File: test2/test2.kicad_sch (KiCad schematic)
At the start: 2 parts

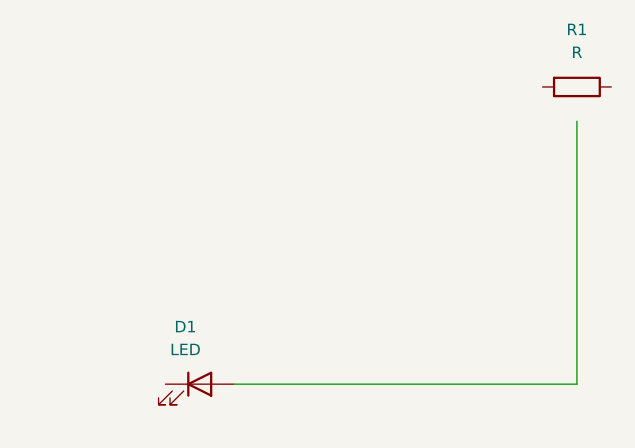
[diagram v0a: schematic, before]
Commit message: 2 Reference Changed and  1 value changed
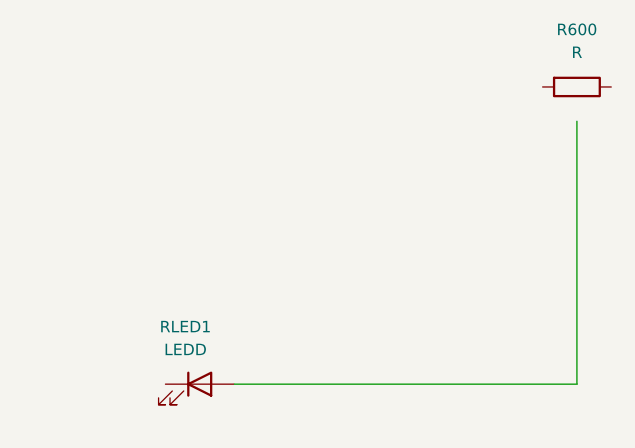
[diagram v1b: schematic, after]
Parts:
- RLED1: renamed from D1; value LED -> LEDD
- renumbered R1 to R600
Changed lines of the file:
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@@
 		(dnp no)
 		(fields_autoplaced yes)
-		(property "Reference" "R1"
+		(property "Reference" "R600"
 			(at 144.78 78.74 90)
 			(show_name no)
@@
 			(project "test2"
 				(path "/a16b2917-54e0-4f71-a869-9bcc0622af1e"
-					(reference "R1")
+					(reference "R600")
 					(unit 1)
 				)
@@
 		(dnp no)
 		(fields_autoplaced yes)
-		(property "Reference" "D1"
+		(property "Reference" "RLED1"
 			(at 101.2825 111.76 0)
 			(show_name no)
@@
 			)
 		)
-		(property "Value" "LED"
+		(property "Value" "LEDD"
 			(at 101.2825 114.3 0)
 			(show_name no)
@@
 			(project "test2"
 				(path "/a16b2917-54e0-4f71-a869-9bcc0622af1e"
-					(reference "D1")
+					(reference "RLED1")
 					(unit 1)
 				)

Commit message: Changed DNP in one changed footprint in other
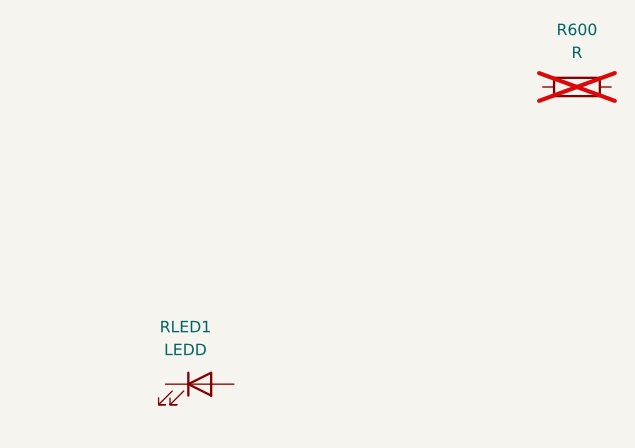
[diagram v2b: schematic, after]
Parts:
- R600: now not fitted; now left out of the parts list
- RLED1: footprint (none) -> Battery:BatteryClip_Keystone_54_D16-19mm
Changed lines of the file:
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@@
 		(comment 5 "c1000")
-	)
-	(wire
-		(pts
-			(xy 106.68 118.11) (xy 144.78 118.11)
-		)
-		(stroke
-			(width 0)
-			(type default)
-		)
-	)
-	(wire
-		(pts
-			(xy 144.78 118.11) (xy 144.78 88.9)
-		)
-		(stroke
-			(width 0)
-			(type default)
-		)
 	)
 	(symbol
@@
 		(body_style 1)
 		(exclude_from_sim no)
-		(in_bom yes)
-		(on_board yes)
+		(in_bom no)
+		(on_board no)
 		(in_pos_files yes)
-		(dnp no)
+		(dnp yes)
 		(fields_autoplaced yes)
 		(property "Reference" "R600"
@@
 			)
 		)
-		(property "Footprint" ""
+		(property "Footprint" "Battery:BatteryClip_Keystone_54_D16-19mm"
 			(at 102.87 118.11 0)
 			(hide yes)

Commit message: Removed 2 symbols
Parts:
- removed R600: R, symbol Device:R
- removed RLED1: LEDD, Battery:BatteryClip_Keystone_54_D16-19mm, symbol Device:LED
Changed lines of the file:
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@@
 		(comment 5 "c1000")
-	)
-	(symbol
-		(lib_id "Device:R")
-		(at 144.78 85.09 270)
-		(unit 1)
-		(body_style 1)
-		(exclude_from_sim no)
-		(in_bom no)
-		(on_board no)
-		(in_pos_files yes)
-		(dnp yes)
-		(fields_autoplaced yes)
-		(property "Reference" "R600"
-			(at 144.78 78.74 90)
-			(show_name no)
-			(do_not_autoplace no)
-			(effects
-				(font
-					(size 1.27 1.27)
-				)
-			)
-		)
-		(property "Value" "R"
-			(at 144.78 81.28 90)
-			(show_name no)
-			(do_not_autoplace no)
-			(effects
-				(font
-					(size 1.27 1.27)
-				)
-			)
-		)
-		(property "Footprint" ""
-			(at 144.78 83.312 90)
-			(hide yes)
-			(show_name no)
-			(do_not_autoplace no)
-			(effects
-				(font
-					(size 1.27 1.27)
-				)
-			)
-		)
-		(property "Datasheet" ""
-			(at 144.78 85.09 0)
-			(hide yes)
-			(show_name no)
-			(do_not_autoplace no)
-			(effects
-				(font
-					(size 1.27 1.27)
-				)
-			)
-		)
-		(property "Description" "Resistor"
-			(at 144.78 85.09 0)
-			(hide yes)
-			(show_name no)
-			(do_not_autoplace no)
-			(effects
-				(font
-					(size 1.27 1.27)
-				)
-			)
-		)
-		(pin "2"
-		)
-		(pin "1"
-		)
-		(instances
-			(project "test2"
-				(path "/a16b2917-54e0-4f71-a869-9bcc0622af1e"
-					(reference "R600")
-					(unit 1)
-				)
-			)
-		)
-	)
-	(symbol
-		(lib_id "Device:LED")
-		(at 102.87 118.11 0)
-		(unit 1)
-		(body_style 1)
-		(exclude_from_sim no)
-		(in_bom yes)
-		(on_board yes)
-		(in_pos_files yes)
-		(dnp no)
-		(fields_autoplaced yes)
-		(property "Reference" "RLED1"
-			(at 101.2825 111.76 0)
-			(show_name no)
-			(do_not_autoplace no)
-			(effects
-				(font
-					(size 1.27 1.27)
-				)
-			)
-		)
-		(property "Value" "LEDD"
-			(at 101.2825 114.3 0)
-			(show_name no)
-			(do_not_autoplace no)
-			(effects
-				(font
-					(size 1.27 1.27)
-				)
-			)
-		)
-		(property "Footprint" "Battery:BatteryClip_Keystone_54_D16-19mm"
-			(at 102.87 118.11 0)
-			(hide yes)
-			(show_name no)
-			(do_not_autoplace no)
-			(effects
-				(font
-					(size 1.27 1.27)
-				)
-			)
-		)
-		(property "Datasheet" ""
-			(at 102.87 118.11 0)
-			(hide yes)
-			(show_name no)
-			(do_not_autoplace no)
-			(effects
-				(font
-					(size 1.27 1.27)
-				)
-			)
-		)
-		(property "Description" "Light emitting diode"
-			(at 102.87 118.11 0)
-			(hide yes)
-			(show_name no)
-			(do_not_autoplace no)
-			(effects
-				(font
-					(size 1.27 1.27)
-				)
-			)
-		)
-		(property "Sim.Pins" "1=K 2=A"
-			(at 102.87 118.11 0)
-			(hide yes)
-			(show_name no)
-			(do_not_autoplace no)
-			(effects
-				(font
-					(size 1.27 1.27)
-				)
-			)
-		)
-		(pin "2"
-		)
-		(pin "1"
-		)
-		(instances
-			(project "test2"
-				(path "/a16b2917-54e0-4f71-a869-9bcc0622af1e"
-					(reference "RLED1")
-					(unit 1)
-				)
-			)
-		)
 	)
 	(sheet_instances

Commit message: 2 symbols + 1 wire
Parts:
- added D1: LED, symbol Device:LED
- added R1: R, symbol Device:R
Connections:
- new net: D1.1 (K), R1.1
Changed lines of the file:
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@@
 		(comment 5 "c1000")
+	)
+	(wire
+		(pts
+			(xy 128.27 115.57) (xy 128.27 119.38)
+		)
+		(stroke
+			(width 0)
+			(type default)
+		)
+	)
+	(wire
+		(pts
+			(xy 83.82 115.57) (xy 128.27 115.57)
+		)
+		(stroke
+			(width 0)
+			(type default)
+		)
+	)
+	(symbol
+		(lib_id "Device:LED")
+		(at 132.08 119.38 0)
+		(unit 1)
+		(body_style 1)
+		(exclude_from_sim no)
+		(in_bom yes)
+		(on_board yes)
+		(in_pos_files yes)
+		(dnp no)
+		(fields_autoplaced yes)
+		(property "Reference" "D1"
+			(at 130.4925 113.03 0)
+			(show_name no)
+			(do_not_autoplace no)
+			(effects
+				(font
+					(size 1.27 1.27)
+				)
+			)
+		)
+		(property "Value" "LED"
+			(at 130.4925 115.57 0)
+			(show_name no)
+			(do_not_autoplace no)
+			(effects
+				(font
+					(size 1.27 1.27)
+				)
+			)
+		)
+		(property "Footprint" ""
+			(at 132.08 119.38 0)
+			(hide yes)
+			(show_name no)
+			(do_not_autoplace no)
+			(effects
+				(font
+					(size 1.27 1.27)
+				)
+			)
+		)
+		(property "Datasheet" ""
+			(at 132.08 119.38 0)
+			(hide yes)
+			(show_name no)
+			(do_not_autoplace no)
+			(effects
+				(font
+					(size 1.27 1.27)
+				)
+			)
+		)
+		(property "Description" "Light emitting diode"
+			(at 132.08 119.38 0)
+			(hide yes)
+			(show_name no)
+			(do_not_autoplace no)
+			(effects
+				(font
+					(size 1.27 1.27)
+				)
+			)
+		)
+		(property "Sim.Pins" "1=K 2=A"
+			(at 132.08 119.38 0)
+			(hide yes)
+			(show_name no)
+			(do_not_autoplace no)
+			(effects
+				(font
+					(size 1.27 1.27)
+				)
+			)
+		)
+		(pin "1"
+		)
+		(pin "2"
+		)
+		(instances
+			(project "test2"
+				(path "/a16b2917-54e0-4f71-a869-9bcc0622af1e"
+					(reference "D1")
+					(unit 1)
+				)
+			)
+		)
+	)
+	(symbol
+		(lib_id "Device:R")
+		(at 83.82 119.38 0)
+		(unit 1)
+		(body_style 1)
+		(exclude_from_sim no)
+		(in_bom yes)
+		(on_board yes)
+		(in_pos_files yes)
+		(dnp no)
+		(fields_autoplaced yes)
+		(property "Reference" "R1"
+			(at 86.36 118.1099 0)
+			(show_name no)
+			(do_not_autoplace no)
+			(effects
+				(font
+					(size 1.27 1.27)
+				)
+				(justify left)
+			)
+		)
+		(property "Value" "R"
+			(at 86.36 120.6499 0)
+			(show_name no)
+			(do_not_autoplace no)
+			(effects
+				(font
+					(size 1.27 1.27)
+				)
+				(justify left)
+			)
+		)
+		(property "Footprint" ""
+			(at 82.042 119.38 90)
+			(hide yes)
+			(show_name no)
+			(do_not_autoplace no)
+			(effects
+				(font
+					(size 1.27 1.27)
+				)
+			)
+		)
+		(property "Datasheet" ""
+			(at 83.82 119.38 0)
+			(hide yes)
+			(show_name no)
+			(do_not_autoplace no)
+			(effects
+				(font
+					(size 1.27 1.27)
+				)
+			)
+		)
+		(property "Description" "Resistor"
+			(at 83.82 119.38 0)
+			(hide yes)
+			(show_name no)
+			(do_not_autoplace no)
+			(effects
+				(font
+					(size 1.27 1.27)
+				)
+			)
+		)
+		(pin "2"
+		)
+		(pin "1"
+		)
+		(instances
+			(project "test2"
+				(path "/a16b2917-54e0-4f71-a869-9bcc0622af1e"
+					(reference "R1")
+					(unit 1)
+				)
+			)
+		)
 	)
 	(sheet_instances
